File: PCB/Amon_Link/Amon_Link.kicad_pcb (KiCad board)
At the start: 4 copper layers, 80 x 40 mm, 103 parts, among them IC1 SPX5205M5-L/TR, J1 USB_C_Receptacle_USB2.0, J2 SMA Edge, J3 Programing port, J4 SMA Edge, SW1 SW_SPST, U1 CH32V003F4P6, U2 CH340G, U3 NRF24L01, U4 RFX2401C, U5 NRF24L01, U6 RFX2401C, Y1 12MHz, Y2 12MHz, Y3 16MHz, Y4 16MHz

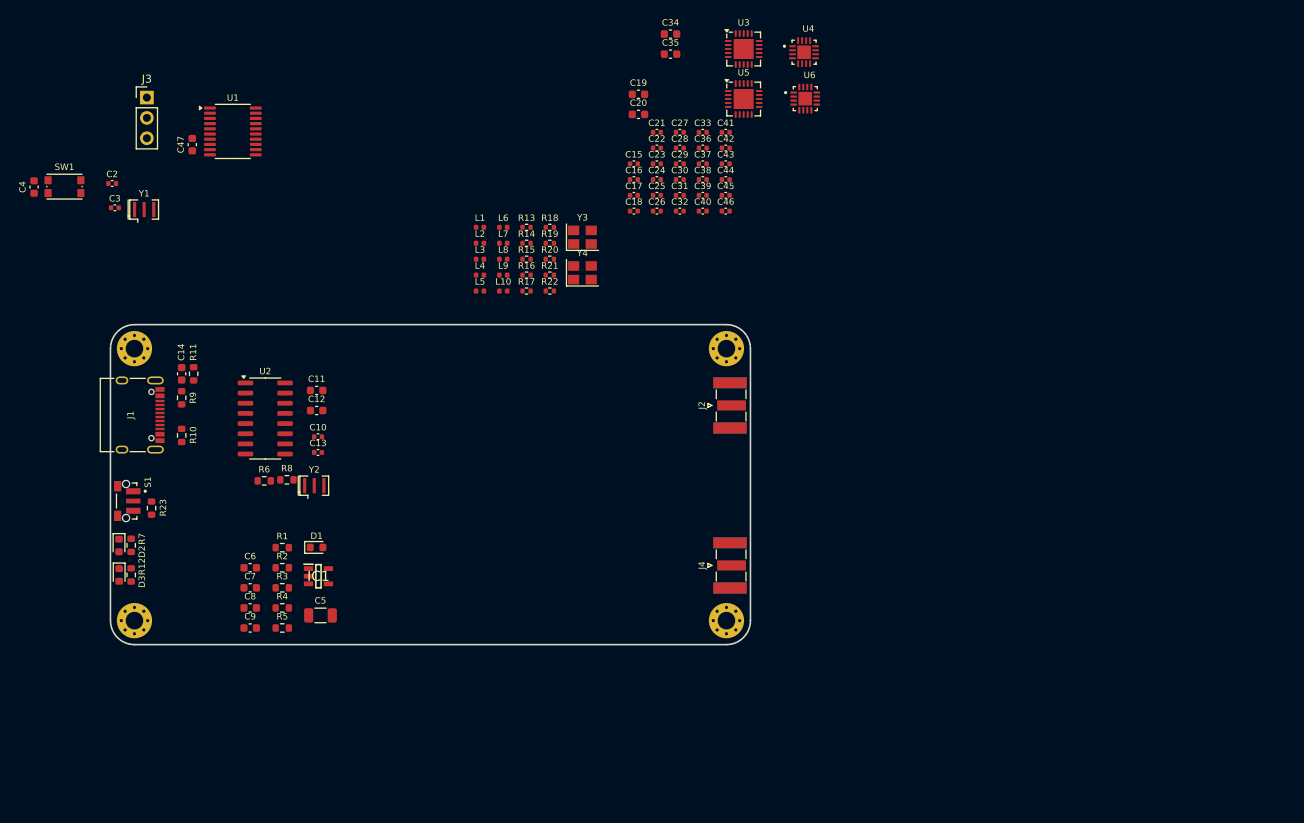
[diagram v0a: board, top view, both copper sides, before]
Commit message: shematic done, layout in progress
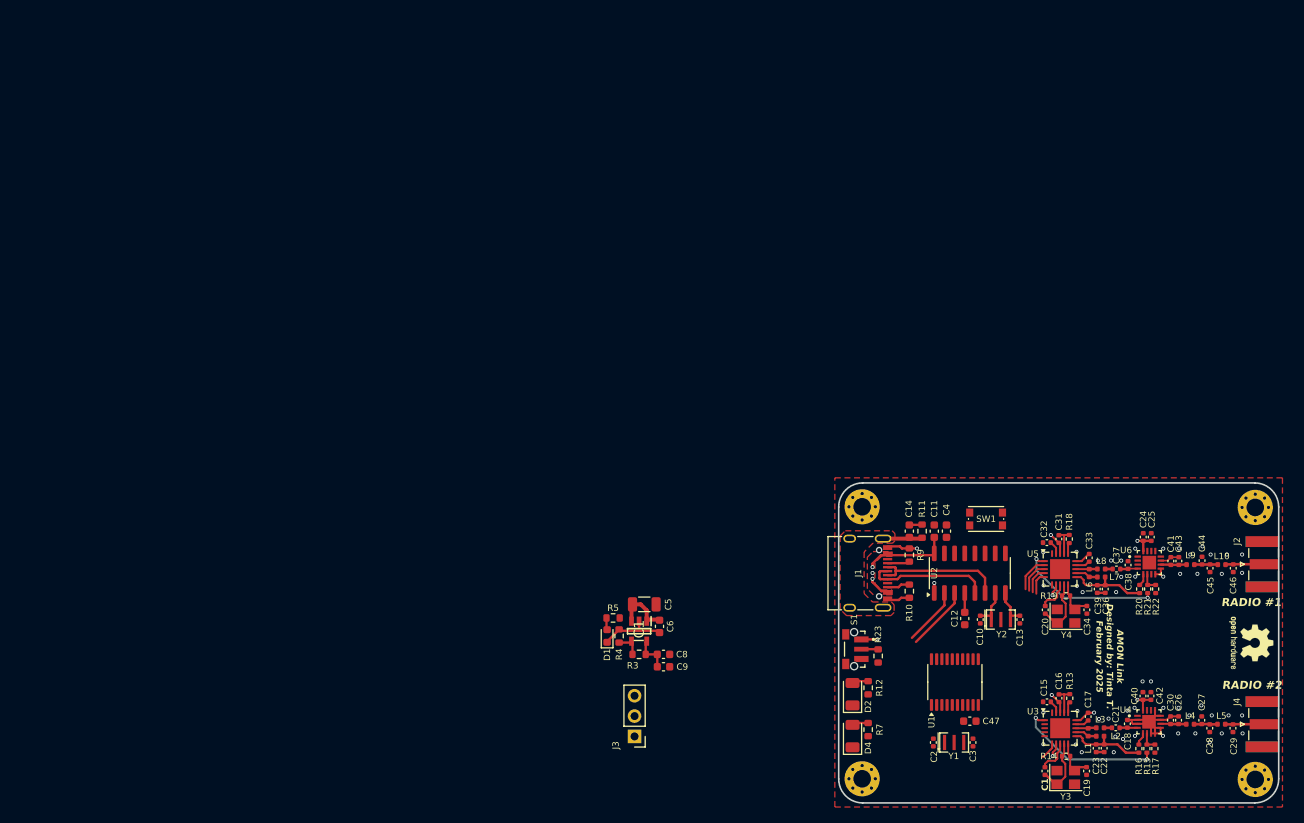
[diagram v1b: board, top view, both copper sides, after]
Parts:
- removed C35: 22pF, Capacitor_SMD:C_0603_1608Metric
- removed C7: 10nF, Capacitor_SMD:C_0603_1608Metric
- removed D3: RED, LED_SMD:LED_0603_1608Metric
- removed R1, R2: 500k, Resistor_SMD:R_0603_1608Metric
- removed R6, R8: 0, Resistor_SMD:R_0603_1608Metric
- added C1: 22pF, Capacitor_SMD:C_0402_1005Metric, F.Cu at (152.0, 110.5)
- added D4: RED, LED_SMD:LED_1206_3216Metric, F.Cu at (128.0, 106.1)
- added REF**: OSHW-Logo2_7.3x6mm_SilkScreen, Symbol:OSHW-Logo2_7.3x6mm_SilkScreen, F.Cu at (177.8, 94.5)
- C19, C20, C34: footprint Capacitor_SMD:C_0603_1608Metric -> Capacitor_SMD:C_0402_1005Metric
- D2: value RED -> BLUE; footprint LED_SMD:LED_0603_1608Metric -> LED_SMD:LED_1206_3216Metric
- moved C3 126.4 mm to (143.0, 106.9), turned to -90 degrees
- moved C2 124.2 mm to (138.1, 106.9), turned to -90 degrees
- moved SW1 122.5 mm to (144.7, 79.0)
- moved C4 121.9 mm to (139.7, 80.5)
- moved Y1 121.2 mm to (140.7, 106.9)
- moved C47 121.0 mm to (142.6, 104.3), turned to 180 degrees
- moved U1 113.5 mm to (140.8, 99.4), turned to 90 degrees
- moved L5 107.3 mm to (174.1, 104.7)
- moved L4 105.0 mm to (170.2, 104.7)
- moved C19 101.5 mm to (157.2, 110.5), turned to 90 degrees
- moved J3 100.5 mm to (100.7, 106.2), turned to 180 degrees
- moved L2 99.0 mm to (158.9, 106.2)
- moved L1 98.8 mm to (157.4, 105.7), turned to 90 degrees
- moved C29 98.8 mm to (175.5, 105.2), turned to -90 degrees
- moved R15 98.8 mm to (164.8, 107.7), turned to 90 degrees
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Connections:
- C10 pad 1: Net-(U2-XI) -> GND
- C10 pad 2: GND -> Net-(U2-XI)
- C13 pad 1: Net-(U2-XO) -> GND
- C13 pad 2: GND -> Net-(U2-XO)
- C19 pad 1: Net-(U3-XC2) -> GND
- C19 pad 2: GND -> Net-(U3-XC1)
- C20 pad 1: Net-(U3-XC1) -> GND
- C20 pad 2: GND -> Net-(U5-XC2)
- C34 pad 1: Net-(U5-XC2) -> GND
- C34 pad 2: GND -> Net-(U5-XC1)
- R12 pad 1: Net-(D3-A) -> Net-(D2-A)
- R7 pad 1: Net-(D2-A) -> Net-(D4-A)
- U1 pad 10: /IRQ1 -> /LED_RED
- U1 pad 19: /LED_RED -> /IRQ1
- U1 pad 20: /LED_BLUE -> /IRQ2
- U1 pad 8: /IRQ2 -> /LED_BLUE
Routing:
- net GND: track 0.00 -> 62.1 mm, vias 0 -> 54
- net +3.3V: track 0.00 -> 26.3 mm, vias 0 -> 8
- net +5V: track 0.00 -> 20.8 mm, vias 0 -> 3
- net /CE1: track 0.00 -> 18.8 mm, vias 0 -> 2
- net /CE2: track 0.00 -> 18.5 mm, vias 0 -> 2
- net /D-: track 0.00 -> 16.3 mm
- net /D+: track 0.00 -> 15.7 mm
- net Net-(U5-VDD_PA): track 0.00 -> 10.1 mm
- net Net-(U3-VDD_PA): track 0.00 -> 9.99 mm
- net /RXD: track 0.00 -> 8.11 mm
- net Net-(U3-XC2): track 0.00 -> 7.88 mm
- net Net-(U5-XC2): track 0.00 -> 7.71 mm
- net /TXD: track 0.00 -> 7.29 mm
- net Net-(U3-XC1): track 0.00 -> 5.38 mm
- net Net-(U5-XC1): track 0.00 -> 5.13 mm
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- added copper zone on F.Cu, net +5V
- added copper zone on F.Cu, net GND
- added copper zone on F.Cu, net Net-(J1-SHIELD)
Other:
- board size 80 x 40 mm -> 55 x 40 mm
- board text added: "AMON Link Designed by: Tinta T. February 2025"
- board text added: "RADIO #1"
- board text added: "RADIO #2"

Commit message: pcb update and case
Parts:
- added R1: 10k, Resistor_SMD:R_0603_1608Metric, F.Cu at (142.8, 94.9)
- added R2: 10k, Resistor_SMD:R_0603_1608Metric, F.Cu at (148.6, 98.1)
- moved J3 42.6 mm to (143.0, 111.4), turned to -90 degrees
- moved D1 39.5 mm to (136.7, 91.1), turned to -90 degrees
- moved R5 37.0 mm to (135.1, 91.1), turned to 90 degrees
- moved REF** 35.8 mm to (145.9, 78.3), turned to 0 degrees
- moved R3 35.1 mm to (136.0, 100.7)
- moved IC1 35.1 mm to (136.0, 97.8)
- moved C6 35.0 mm to (138.6, 97.2)
- moved R4 35.0 mm to (133.5, 98.4)
- moved C5 35.0 mm to (136.7, 93.7)
- moved C8 32.3 mm to (136.0, 102.2), turned to 180 degrees
- moved C9 32.3 mm to (136.0, 103.8), turned to 180 degrees
- moved SW1 29.4 mm to (136.0, 107.1), turned to 180 degrees
- moved C4 26.6 mm to (139.6, 107.1), turned to -90 degrees
- moved C47 3.70 mm to (146.3, 104.6)
- moved C3 3.56 mm to (146.6, 107.3)
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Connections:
- U1 pad 11: /CE2 -> /IRQ2
- U1 pad 12: /CE1 -> /CE2
- U1 pad 13: /CSN2 -> /CE1
- U1 pad 19: /IRQ1 -> /CSN2
- U1 pad 20: /IRQ2 -> /IRQ1
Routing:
- net /LED_BLUE: track 0.00 -> 31.9 mm
- net /MISO: track 2.86 -> 34.3 mm, vias 0 -> 2
- net /MOSI: track 3.44 -> 32.4 mm, vias 0 -> 2
- net /LED_RED: track 0.00 -> 27.7 mm
- net /SCK: track 4.02 -> 30.4 mm
- net /BTN: track 2.11 -> 22.9 mm
- net GND: track 62.1 -> 81.9 mm, vias 54 -> 420
- net /IRQ1: track 2.26 -> 19.6 mm
- net /SWIO: track 0.00 -> 15.5 mm, vias 0 -> 1
- net /CSN2: track 4.60 -> 19.8 mm
- net /CE2: track 18.5 -> 32.4 mm, vias 2 -> 3
- net /CSN1: track 0.00 -> 13.0 mm
- net /IRQ2: track 0.39 -> 12.9 mm
- net /NRST: track 0.00 -> 12.1 mm
- net /CE1: track 18.8 -> 29.7 mm
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- added copper zone on F.Cu, net +3.3V
- added copper zone on In2.Cu, net +5V
- added copper zone on B.Cu, net GND
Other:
- board text added: "GND-SWIO-3V3"
- board text added: "JLCJLCJLCJLC"

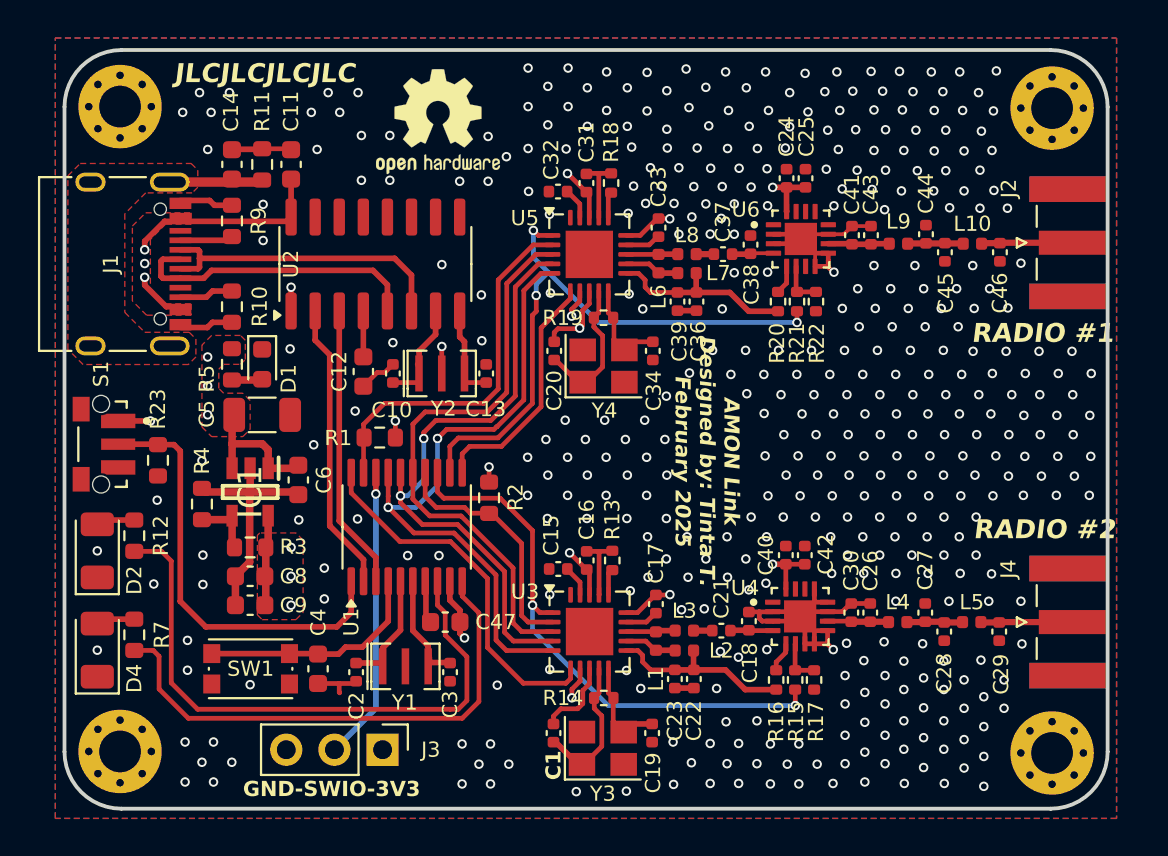
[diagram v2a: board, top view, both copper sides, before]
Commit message: PCB: added graphics, Firmware: USART IRQ working, pinout set
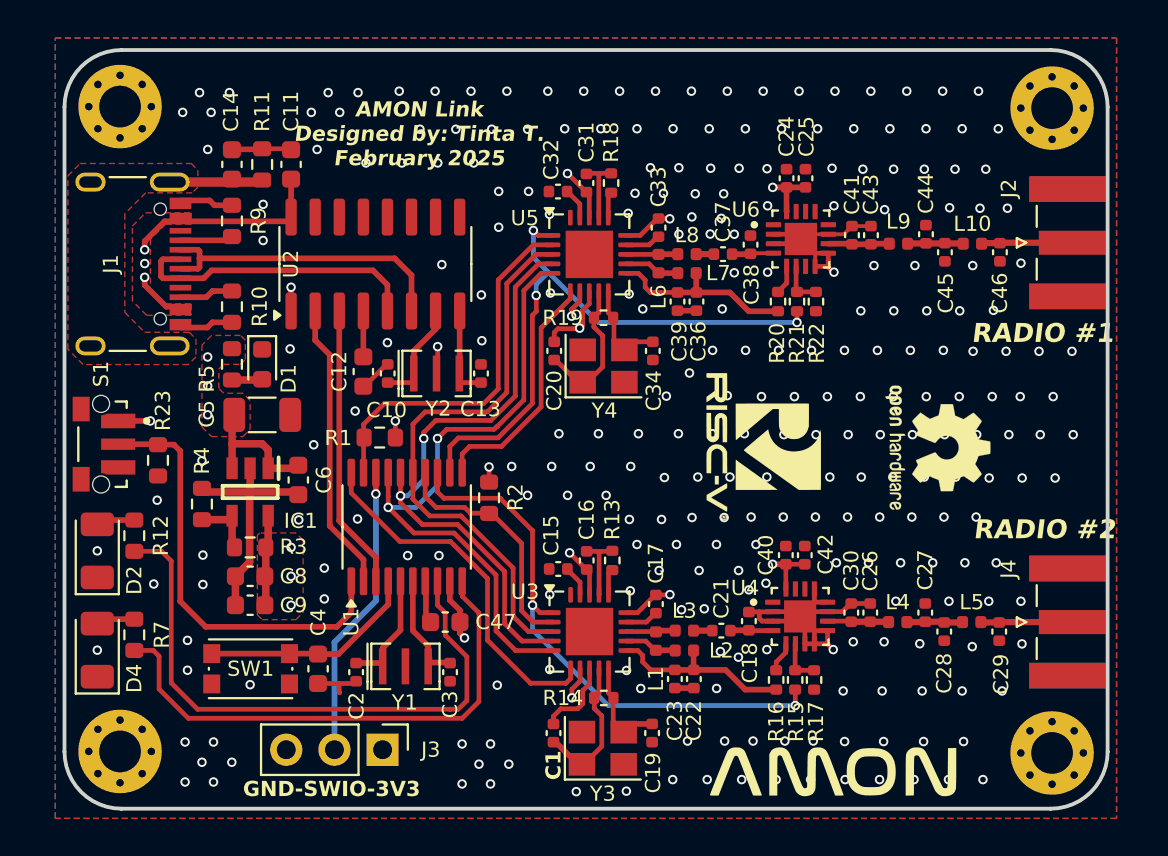
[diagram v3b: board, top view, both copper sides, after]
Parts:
- added G***: LOGO, LOGO:Amon, F.Cu at (166.7, 112.5)
- added G***: LOGO, LOGO:RISC_V, F.Cu at (162.7, 95.3)
- moved REF** 31.5 mm to (172.3, 95.5), turned to -90 degrees
- moved C10 0.27 mm to (143.3, 91.5)
- moved C13 0.27 mm to (148.2, 91.5)
- moved Y2 0.27 mm to (145.8, 91.5)
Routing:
- net /NRST: track 12.1 -> 11.6 mm
- net GND: track 81.9 -> 81.6 mm, vias 420 -> 271

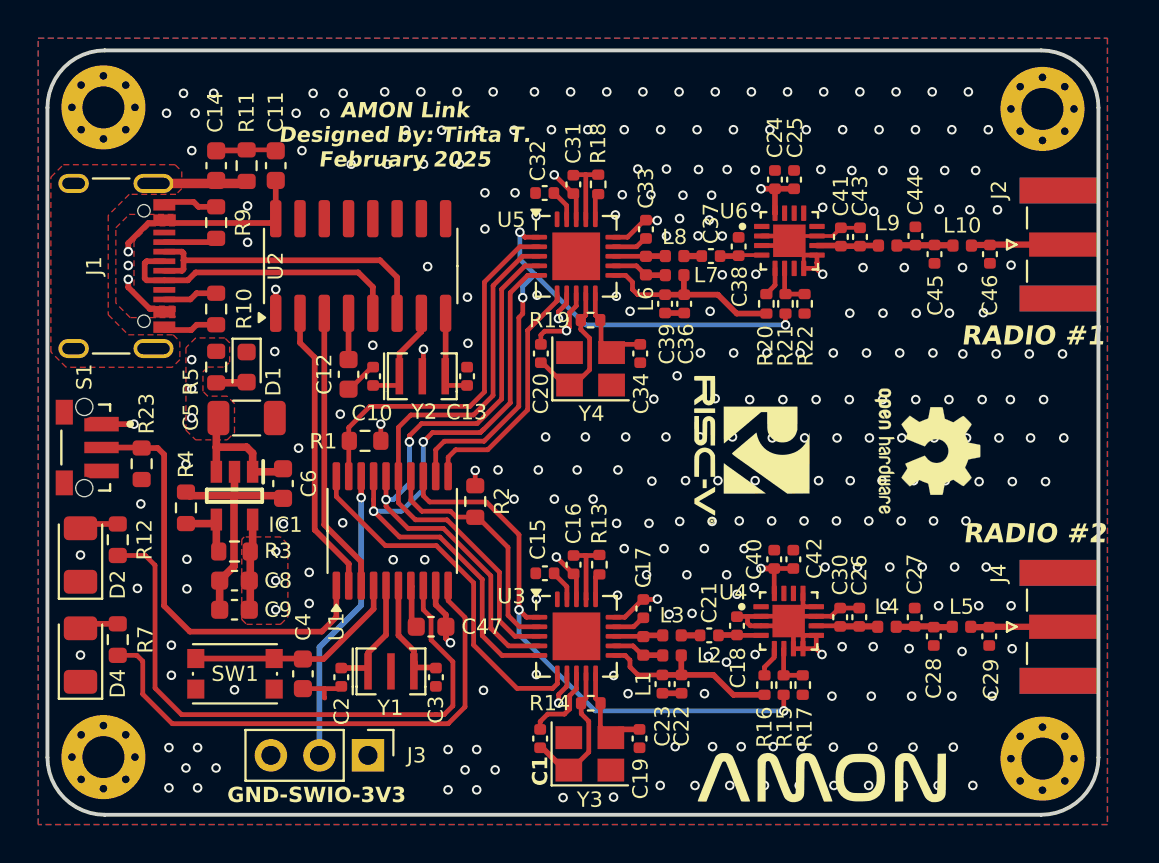
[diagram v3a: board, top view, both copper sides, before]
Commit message: Update
PCB v0.1 complete, firmware in progress
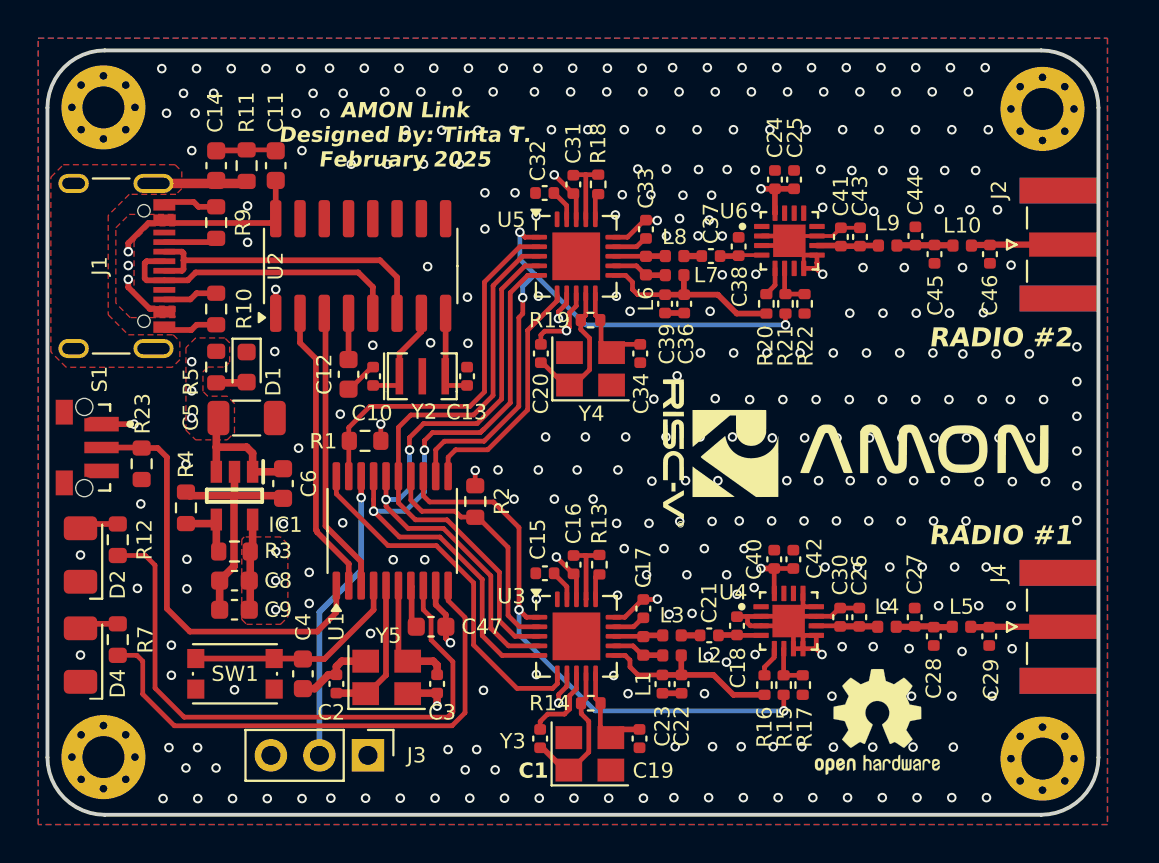
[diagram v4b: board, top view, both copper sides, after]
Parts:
- removed Y1: 12MHz, Crystal:Resonator_SMD_Murata_CSTxExxV-3Pin_3.0x1.1mm
- added Y5: 24MHz, Crystal:Crystal_SMD_3225-4Pin_3.2x2.5mm, F.Cu at (144.0, 107.3)
- moved G*** 18.0 mm to (172.1, 95.4)
- moved REF** 14.4 mm to (169.7, 109.6), turned to 0 degrees
- moved G*** 1.64 mm to (161.1, 95.5)
- moved C2 0.43 mm to (141.3, 107.6), turned to 90 degrees
- moved C3 0.36 mm to (146.6, 107.6)
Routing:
- net GND: track 81.6 -> 84.4 mm, vias 271 -> 311
- net /HSE_IN: track 6.58 -> 7.70 mm
